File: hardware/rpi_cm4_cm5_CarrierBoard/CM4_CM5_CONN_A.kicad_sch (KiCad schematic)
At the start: 67 parts, among them J19 RPI_CMx_A, J6 M20-9990245, J7 2998TR, Q12 2N7002, U19 SN74LVC1G125DBVR, U20 SN74LVC1G07DBVR, U21 MCP7940NT-I/MS, U5 SN74LVC1G125DBVR, Y2 32.768kHz

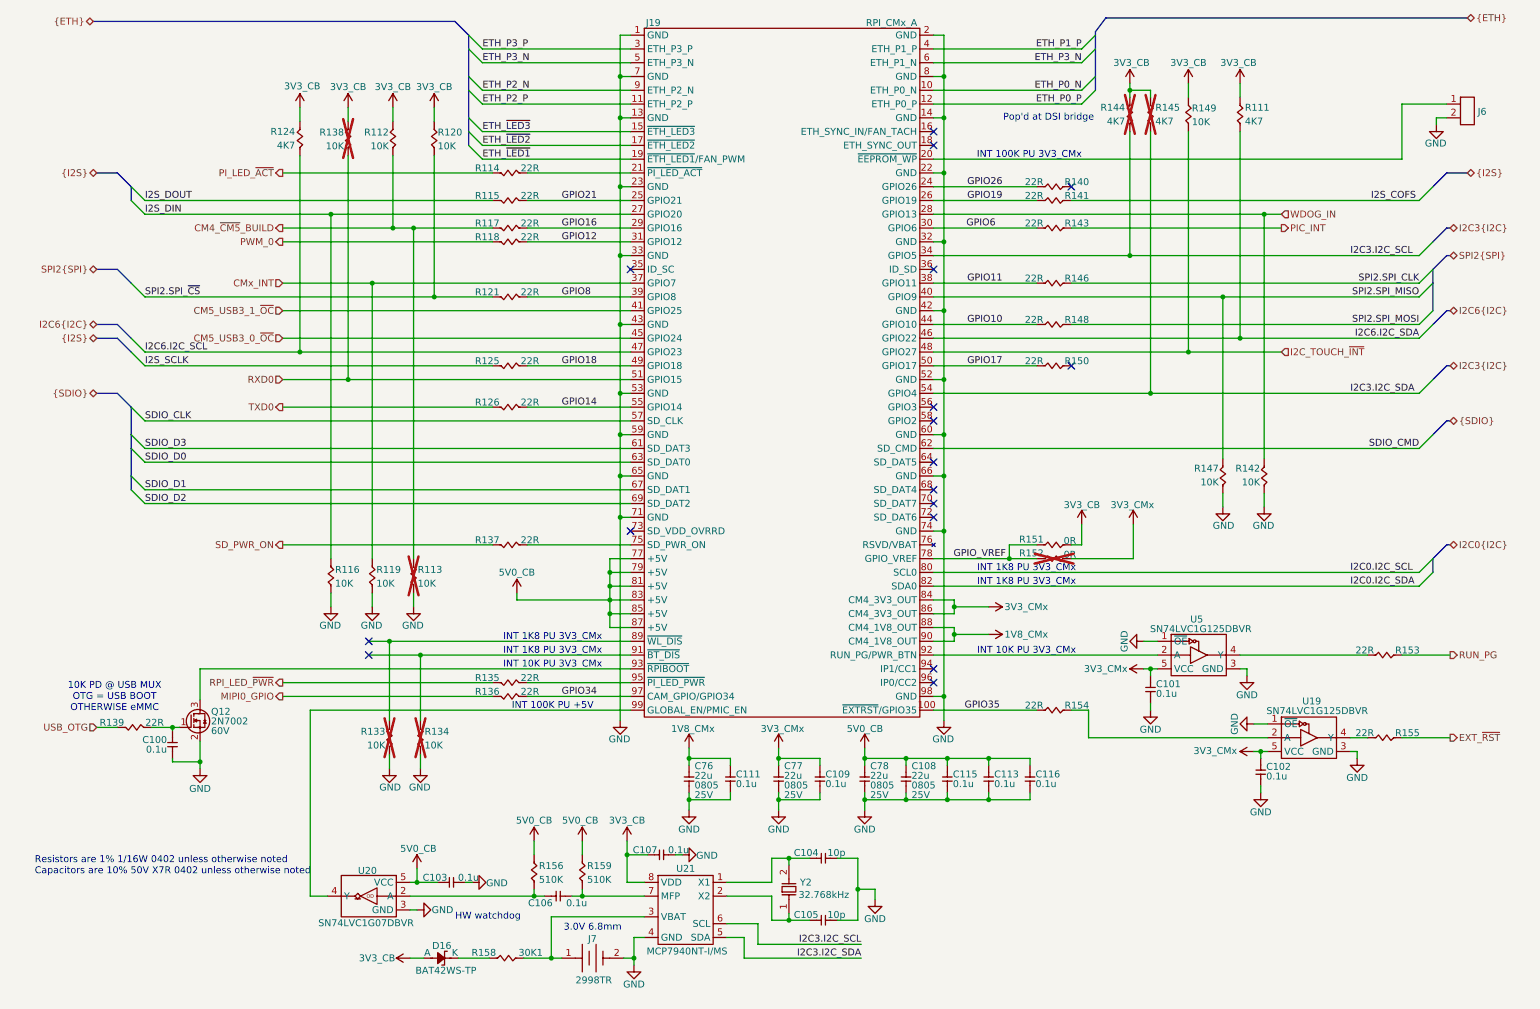
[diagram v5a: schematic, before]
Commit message: Update watchdog timer circuit to add external watchdog timer IC to be fed by PIC Adjust reset scheme in power supply sheet accordingly Adjust PinMux, regen BOM and PDF schematics (preliminary) Start preliminary component placement in the PCB
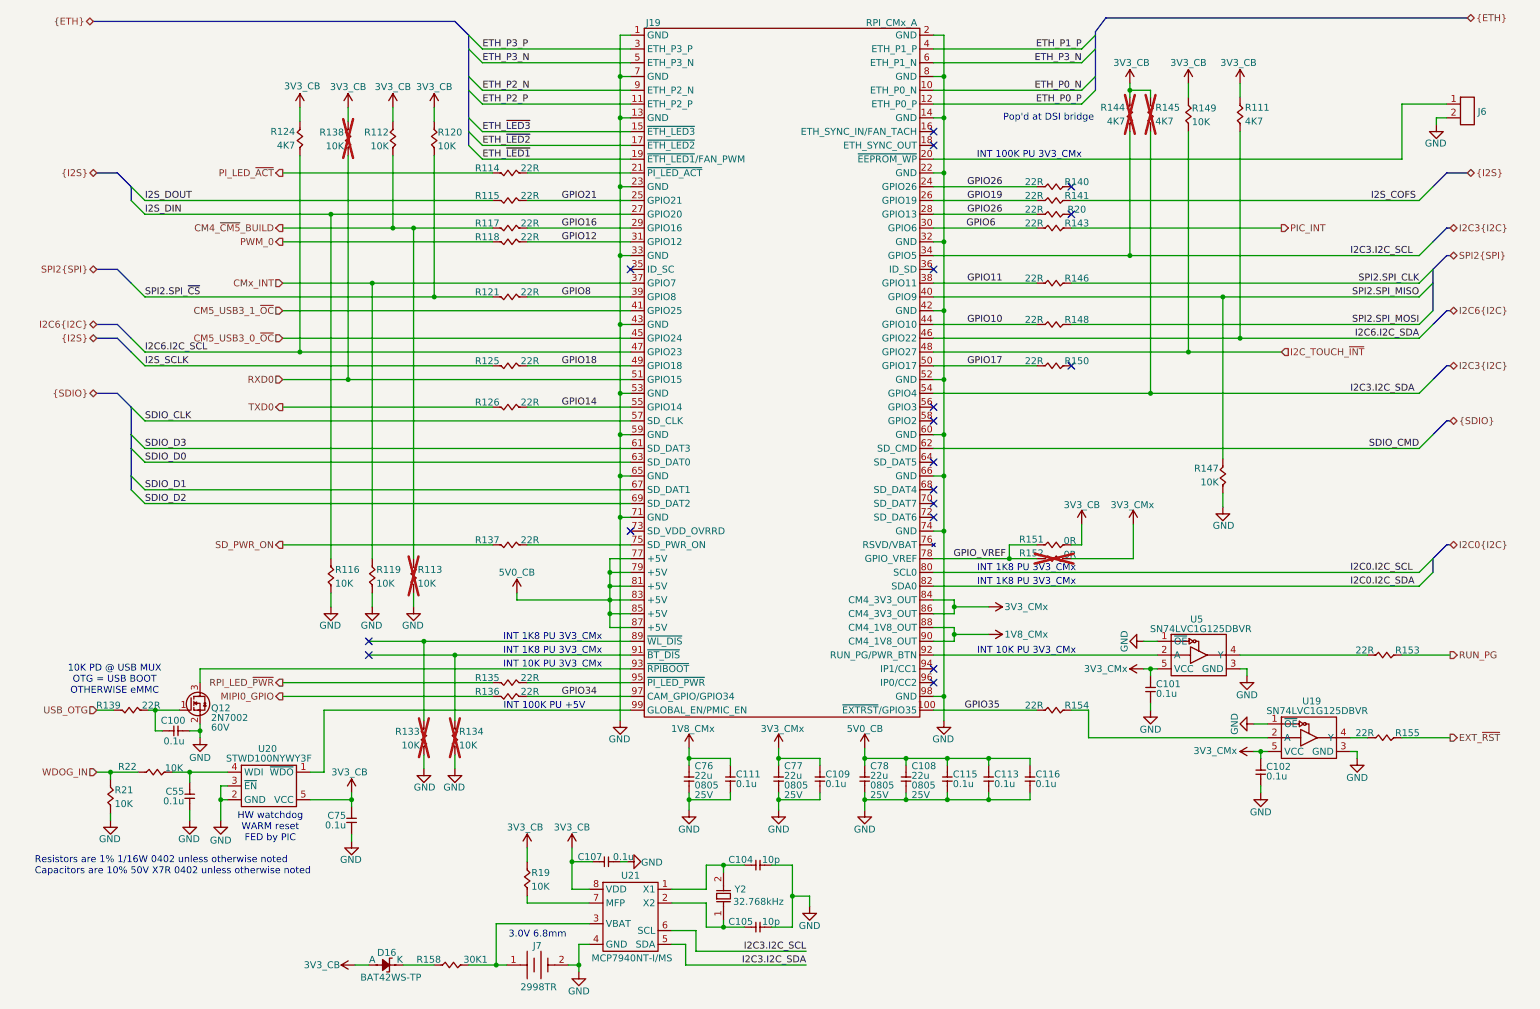
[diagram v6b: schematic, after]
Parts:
- removed C103, C106: 0.1u, footprint:CAP_NONPOL_0402, symbol KicadCompDb:Capacitors/CAP_CER_SMT_00001
- removed R142: 10K, footprint:RES_0402, symbol KicadCompDb:Resistors/RES_SMT_00013
- removed R156, R159: 510K, footprint:RES_0402, symbol KicadCompDb:Resistors/RES_SMT_00020
- removed U20: SN74LVC1G07DBVR, footprint:SOT-23-5, symbol KicadCompDb:Logic/LOGIC_00002
- added C55, C75: 0.1u, footprint:CAP_NONPOL_0402, symbol KicadCompDb:Capacitors/CAP_CER_SMT_00001
- added R19, R21, R22: 10K, footprint:RES_0402, symbol KicadCompDb:Resistors/RES_SMT_00013
- added R20: 22R, footprint:RES_0402, symbol KicadCompDb:Resistors/RES_SMT_00015
- added U20: STWD100NYWY3F, footprint:SOT-23-5, symbol KicadCompDb:Logic/LOGIC_00007
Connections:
- net 3V3_CB: now also C75.2, R19.2, U20.5 (VCC)
- net GND: now also C55.1, C75.1, R21.1, U20.2 (GND), U20.3 (~{EN})
- net GPIO26: now also J19.28 (GPIO13), R20.1
- net WDOG_IN: now also R21.2, R22.2; no longer J19.28 (GPIO13)
- net at J19.99 (GLOBAL_EN/PMIC_EN): now also U20.1 (~{WDO})
- net at U21.7 (MFP): now also R19.1
- new net: C55.2, R22.1, U20.4 (WDI)
- no-connect marks 17 -> 18
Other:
- note added: "HW watchdog WARM reset FED by PIC"
- note removed: "HW watchdog"
- moved on the sheet: C100, C104, C105, C107, D16, J7, Q12, R133, R134, R139, R158, U21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

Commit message: Review watchdog timer circuit to prevent race condition during shutdown
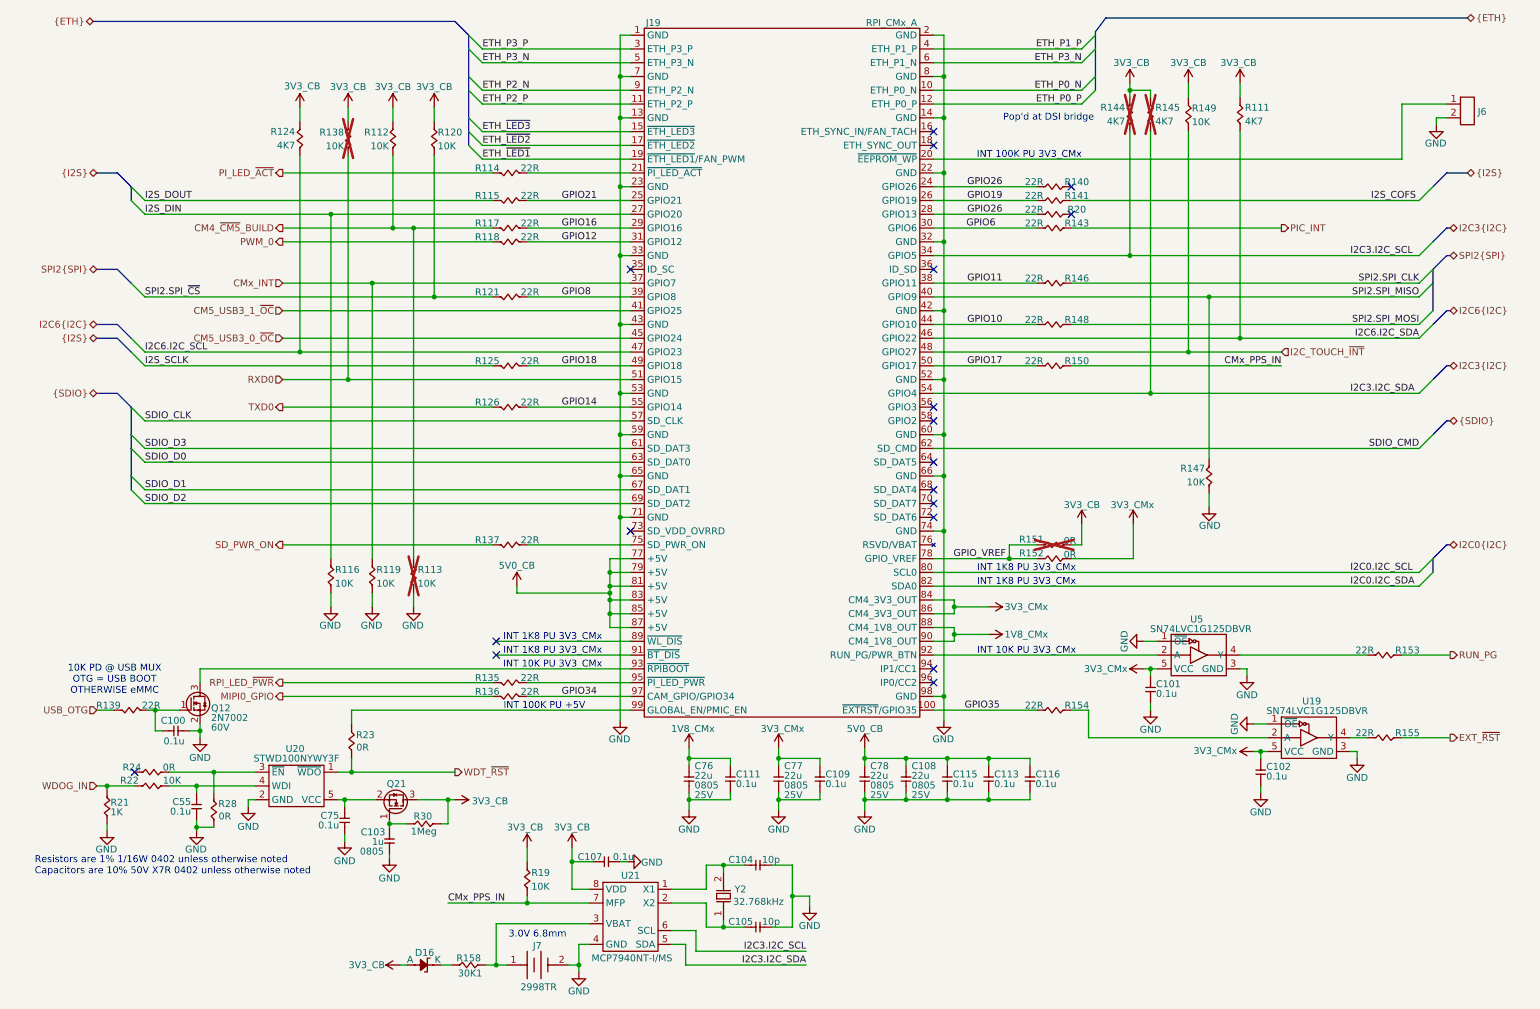
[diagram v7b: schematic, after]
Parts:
- removed R133, R134, R21: 10K, footprint:RES_0402, symbol KicadCompDb:Resistors/RES_SMT_00013
- added C103: 1u, footprint:CAP_NONPOL_0805, symbol KicadCompDb:Capacitors/CAP_CER_SMT_00002
- added Q21: 2N7002, footprint:SOT-23-3, symbol KicadCompDb:Mosfet/MOSFET_00001
- added R21: 1K, footprint:RES_0402, symbol KicadCompDb:Resistors/RES_SMT_00004
- added R23, R24, R28: 0R, footprint:RES_0402, symbol KicadCompDb:Resistors/RES_SMT_00001
- added R30: 1Meg, footprint:RES_0402, symbol KicadCompDb:Resistors/RES_SMT_00006
- R151: now not fitted
- R152: now fitted
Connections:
- net 3V3_CB: now also Q21.3 (D), R30.1; no longer C75.2, U20.5 (VCC)
- net GND: now also C103.1, R21.1, R28.1; no longer U20.3 (~{EN})
- net WDOG_IN: now also R21.2
- net at J19.99 (GLOBAL_EN/PMIC_EN): now also R23.2; no longer U20.1 (~{WDO})
- net CMx_PPS_IN: now reaches R19.1, U21.7 (MFP)
- net CMx_PPS_IN: now also R150.2
- new net: C103.2, Q21.1 (G), R30.2
- new net: C75.2, Q21.2 (S), U20.5 (VCC)
- new net: R24.1, R28.2, U20.3 (~{EN})
- new net WDT_~{RST}: R23.1, U20.1 (~{WDO})
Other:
- note removed: "HW watchdog WARM reset FED by PIC"
- moved on the sheet: C55, D16, R147, R158, R22, U20

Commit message: Finished implementation of watchdog circuit All possible reset scenarios documented
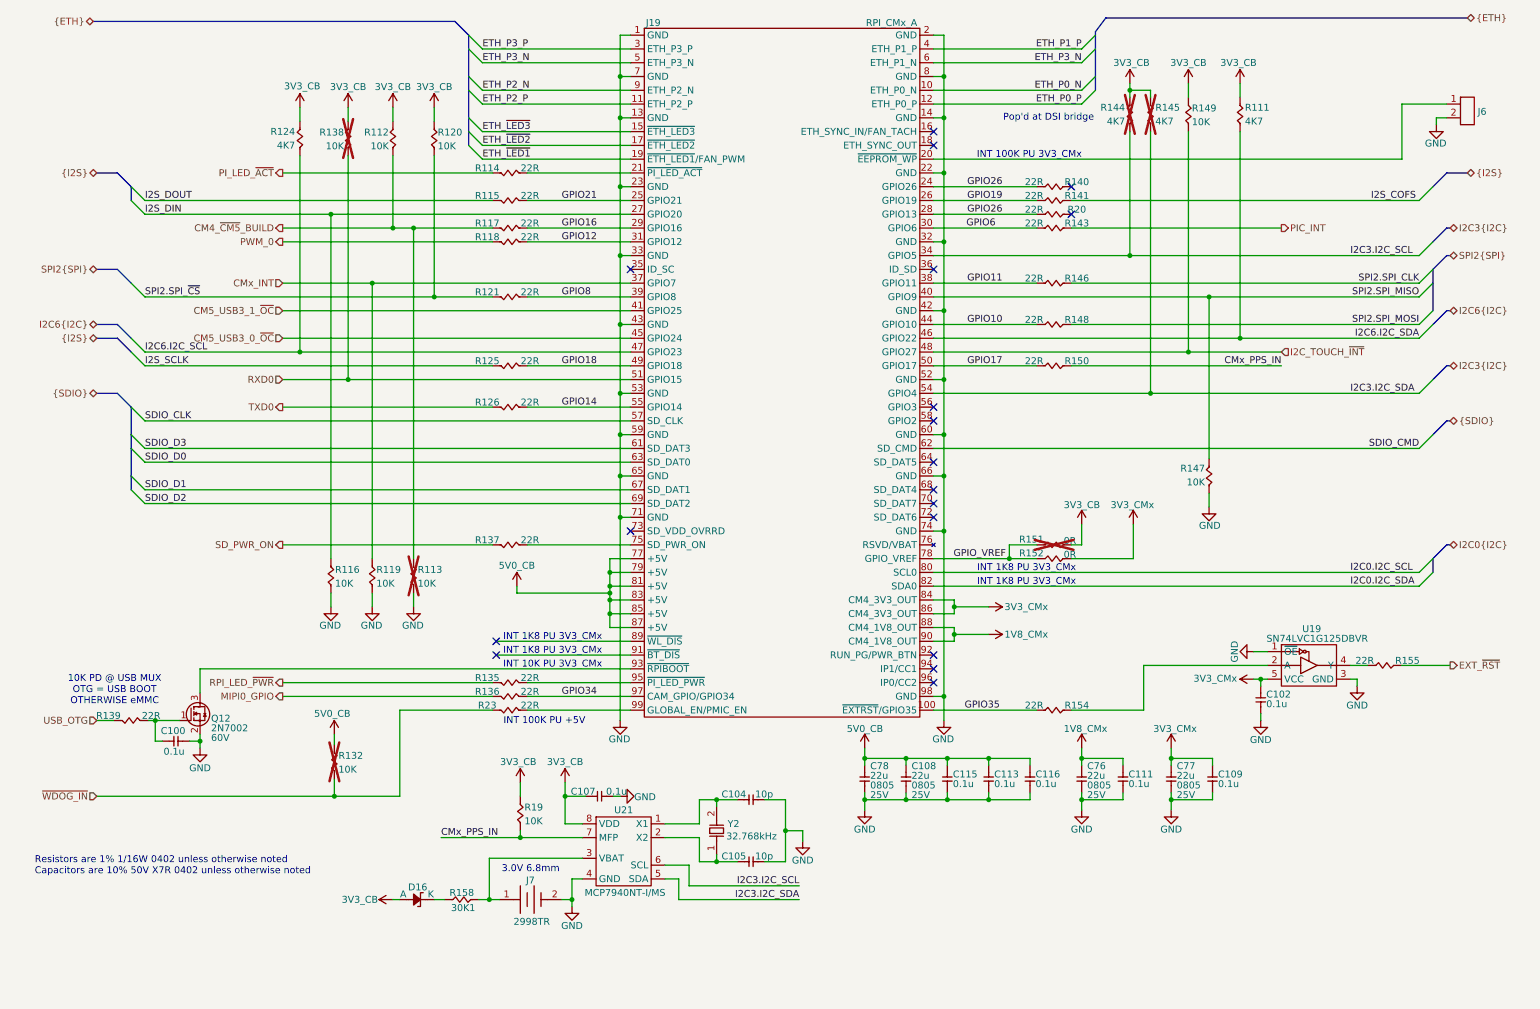
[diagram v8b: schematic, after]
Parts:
- removed C101, C55, C75: 0.1u, footprint:CAP_NONPOL_0402, symbol KicadCompDb:Capacitors/CAP_CER_SMT_00001
- removed C103: 1u, footprint:CAP_NONPOL_0805, symbol KicadCompDb:Capacitors/CAP_CER_SMT_00002
- removed Q21: 2N7002, footprint:SOT-23-3, symbol KicadCompDb:Mosfet/MOSFET_00001
- removed R153: 22R, footprint:RES_0402, symbol KicadCompDb:Resistors/RES_SMT_00015
- removed R21: 1K, footprint:RES_0402, symbol KicadCompDb:Resistors/RES_SMT_00004
- removed R22: 10K, footprint:RES_0402, symbol KicadCompDb:Resistors/RES_SMT_00013
- removed R23, R24, R28: 0R, footprint:RES_0402, symbol KicadCompDb:Resistors/RES_SMT_00001
- removed R30: 1Meg, footprint:RES_0402, symbol KicadCompDb:Resistors/RES_SMT_00006
- removed U20: STWD100NYWY3F, footprint:SOT-23-5, symbol KicadCompDb:Logic/LOGIC_00007
- removed U5: SN74LVC1G125DBVR, footprint:SOT-23-5, symbol KicadCompDb:Logic/LOGIC_00001
- added R132: 10K, footprint:RES_0402, symbol KicadCompDb:Resistors/RES_SMT_00013
- added R23: 22R, footprint:RES_0402, symbol KicadCompDb:Resistors/RES_SMT_00015
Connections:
- net 5V0_CB: now also R132.2
- net at J19.99 (GLOBAL_EN/PMIC_EN): now also R23.1
- new net ~{WDOG_IN}: R132.1, R23.2
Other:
- moved on the sheet: C100, C102, C104, C105, C107, C109, C111, C76, C77, D16, J7, Q12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
